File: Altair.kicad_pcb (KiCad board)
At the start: 2 copper layers, 224.3 x 12.5 mm, 135 parts, among them J1 Battery, SW1 SW_Push, SW10 SW_Push, SW11 SW_Push, SW12 SW_Push, SW13 SW_Push, SW14 SW_Push, SW15 SW_Push, SW16 SW_Push, SW17 SW_Push, SW18 SW_Push, SW19 SW_Push, SW2 SW_Push, SW20 SW_Push, SW21 SW_Push, SW22 SW_Push, SW23 SW_Push, SW24 SW_Push, SW25 SW_Push, SW26 SW_Push, SW27 SW_Push, SW28 SW_Push, SW29 SW_Push, SW3 SW_Push, SW30 SW_Push, SW31 SW_Push, SW32 SW_Push, SW33 SW_Push, SW34 SW_Push, SW35 SW_Push, SW36 SW_Push, SW37 SW_Push, SW38 SW_Push, SW39 SW_Push, SW4 SW_Push, SW40 SW_Push, SW41 SW_Push, SW42 SW_Push, SW43 SW_Push, SW44 SW_Push, SW45 SW_Push, SW46 SW_Push, SW47 SW_Push, SW48 SW_Push, SW49 SW_Push, SW5 SW_Push, SW50 SW_Push, SW51 SW_Push, SW52 SW_Push, SW53 SW_Push, SW54 SW_Push, SW55 SW_Push, SW56 SW_Push, SW57 SW_Push, SW58 SW_Push, SW59 SW_Push, SW6 SW_Push, SW60 SW_Push, SW61 SW_Push, SW62 SW_Push, SW63 SW_Push, SW64 SW_Push, SW7 SW_Push, SW8 SW_Push, SW9 SW_Push, SW97 RST, SW98 PWR, U1 nice_nano

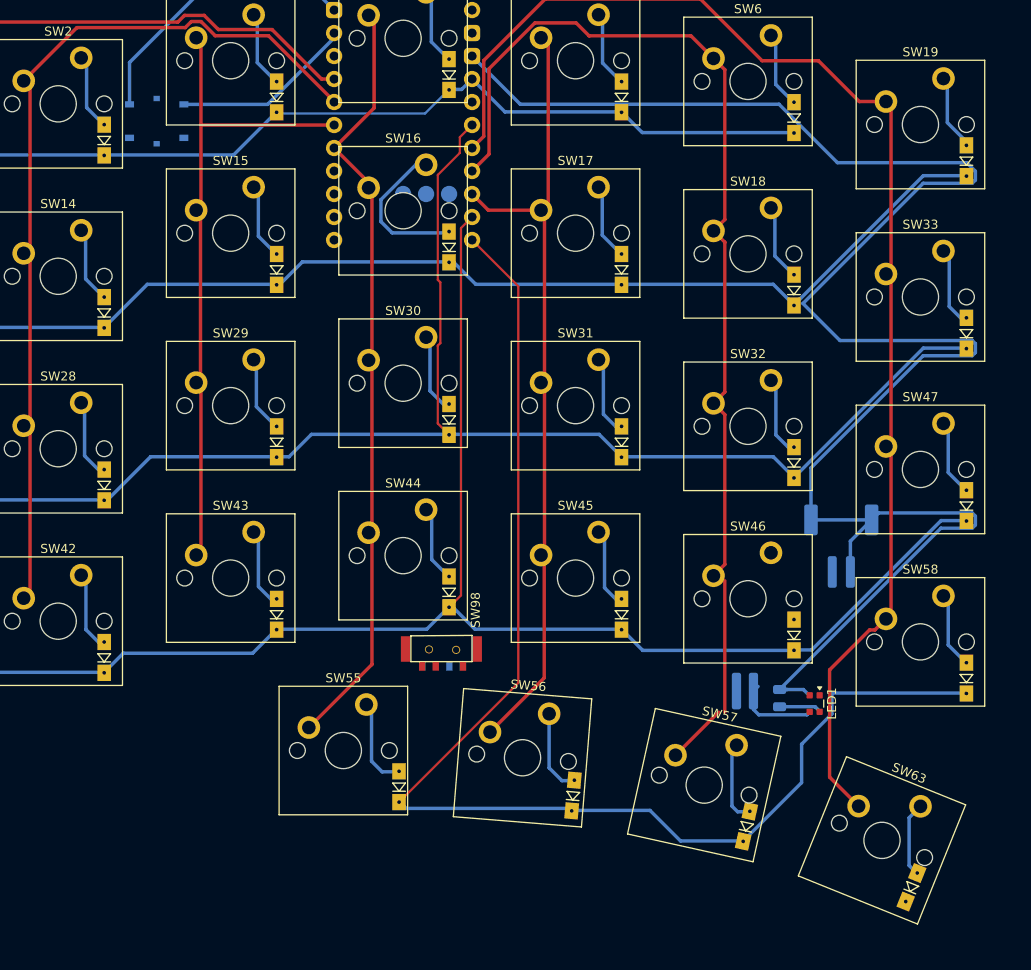
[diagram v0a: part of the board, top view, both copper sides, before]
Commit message: Remove Led
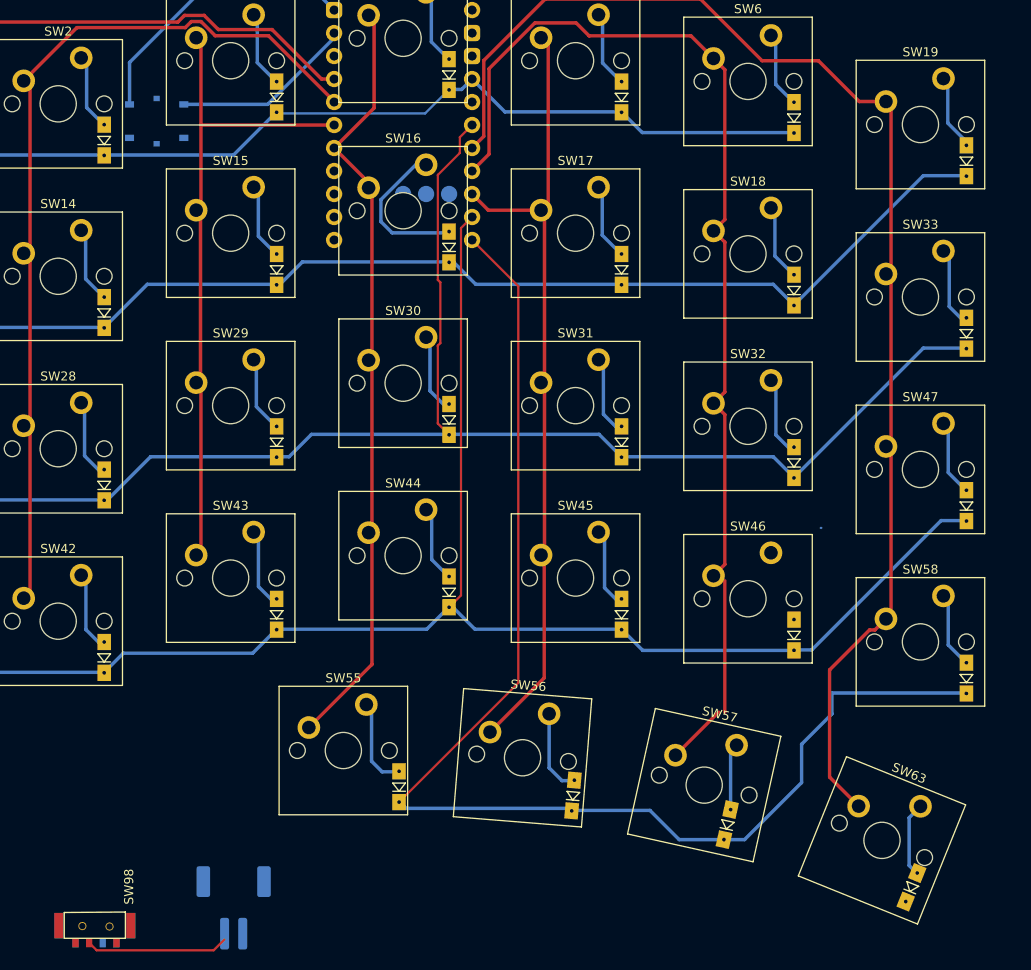
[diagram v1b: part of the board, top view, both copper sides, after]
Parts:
- removed C1: 0.1uF, Capacitor_SMD:C_0805_2012Metric
- removed LED1: WS2812_2020, PCM_marbastlib-various:LED_WS2812_2020
- removed R1: 300R, Resistor_SMD:R_0815_2038Metric
- moved J1 78.1 mm to (76.5, 126.9)
- moved SW98 49.0 mm to (65.1, 127.6)
- moved D57 2.13 mm to (131.1, 117.7)
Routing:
- net GND: track 230.2 -> 31.4 mm
- net Net-(J1-Pin_1): track 0.00 -> 15.8 mm
- net Net-(LED1-DIN): track 9.26 -> 0.00 mm
- net LED1+: track 4.62 -> 0.00 mm
- net N$57: track 9.16 -> 7.38 mm

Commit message: Remove onoff button
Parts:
- removed SW98: PWR, KLOTZ:MSK12C02_reversible
- moved J1 176.3 mm to (-8.38, -27.6), turned to 180 degrees
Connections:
- J1 pad 1: Net-(J1-Pin_1) -> +BATT
- U1 pad 16: LED1+ -> unconnected-(U1-3V3-Pad16)
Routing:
- net Net-(J1-Pin_1): track 15.8 -> 0.00 mm

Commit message: Change Diode Footprint to make new way routing
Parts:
- D1, D10, D11, D12, D13, D14, D15, D16, D17, D18, D19, D2, D20, D21, D22, D23, D24, D25, D26, D27, D28, D29, D3, D30, D31, D32, D33, D34, D35, D36, D37, D38, D39, D4, D40, D41, D42, D43, D44, D45, D46, D47, D48, D49, D5, D50, D51, D52, D53, D54, D55, D56, D57, D58, D59, D6, D60, D61, D62, D63, D64, D7, D8, D9: footprint KLOTZ:Diode_SOD123 -> Diode_SMD:D_SOD-123
- moved SW97 25.5 mm to (53.3, 19.2)
- moved D2 13.6 mm to (48.7, 40.3)
- moved D3 4.42 mm to (80.6, 41.7), turned to 180 degrees
- moved D1 3.69 mm to (46.4, 40.3)
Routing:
- net ROW3: track 169.4 -> 0.00 mm
- net ROW2: track 161.7 -> 0.00 mm
- net COL6: track 145.2 -> 0.00 mm
- net ROW4: track 144.6 -> 0.00 mm
- net ROW1: track 125.2 -> 0.00 mm
- net COL5: track 122.9 -> 0.00 mm
- net COL0: track 117.6 -> 0.00 mm
- net COL1: track 99.3 -> 0.00 mm
- net ROW0: track 101.3 -> 2.30 mm
- net COL4: track 89.1 -> 0.00 mm
- net COL3: track 86.2 -> 0.00 mm
- net COL2: track 73.2 -> 0.00 mm
- net GND: track 31.4 -> 0.00 mm
- net RST: track 20.2 -> 0.00 mm
- net N$16: track 17.1 -> 0.00 mm
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
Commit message: Done routing for SW
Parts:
- removed SW97: RST, PTS526_SMG15_SMTR2_LFS:SW_PTS526_SMG15_SMTR2_LFS
- moved J1 63.0 mm to (46.6, 3.15), turned to -90 degrees
- moved D47 14.4 mm to (144.0, 77.5)
- moved D19 14.3 mm to (144.0, 39.5)
- moved D58 14.2 mm to (144.0, 97.0)
- moved D33 14.2 mm to (144.0, 59.0)
- moved D14 13.2 mm to (49.0, 61.1)
- moved D28 13.2 mm to (49.0, 80.2)
- moved D42 13.2 mm to (49.0, 99.2)
- moved D3 4.25 mm to (81.3, 37.5), turned to 90 degrees
- moved D13 3.32 mm to (46.5, 61.1)
- moved D27 3.32 mm to (46.5, 80.2)
- moved D41 3.32 mm to (46.5, 99.2)
- moved D18 3.09 mm to (141.5, 59.0)
- moved D46 3.08 mm to (141.5, 97.0)
- moved D32 3.08 mm to (141.5, 77.5)
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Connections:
- D10 pad 1: ROW0 -> (no net)
- D11 pad 1: ROW0 -> (no net)
- D12 pad 1: ROW0 -> (no net)
- D19 pad 1: ROW1 -> ROW0
- D20 pad 1: ROW1 -> (no net)
- D21 pad 1: ROW1 -> (no net)
- D22 pad 1: ROW1 -> (no net)
- D23 pad 1: ROW1 -> (no net)
- D24 pad 1: ROW1 -> (no net)
- D25 pad 1: ROW1 -> (no net)
- D26 pad 1: ROW1 -> (no net)
- D33 pad 1: ROW2 -> ROW1
- D34 pad 1: ROW2 -> (no net)
- D35 pad 1: ROW2 -> (no net)
- D36 pad 1: ROW2 -> (no net)
- D37 pad 1: ROW2 -> (no net)
- D38 pad 1: ROW2 -> (no net)
- D39 pad 1: ROW2 -> (no net)
- D40 pad 1: ROW2 -> (no net)
- D47 pad 1: ROW3 -> ROW2
- D48 pad 1: ROW3 -> (no net)
- D49 pad 1: ROW3 -> (no net)
- D50 pad 1: ROW3 -> (no net)
- D51 pad 1: ROW3 -> (no net)
- D52 pad 1: ROW3 -> (no net)
- D53 pad 1: ROW3 -> (no net)
- D54 pad 1: ROW3 -> (no net)
- D58 pad 1: ROW4 -> ROW3
- D59 pad 1: ROW4 -> (no net)
- D60 pad 1: ROW4 -> (no net)
- D61 pad 1: ROW4 -> (no net)
- D62 pad 1: ROW4 -> (no net)
- D63 pad 1: ROW5 -> ROW4
- D7 pad 1: ROW0 -> (no net)
- D8 pad 1: ROW0 -> (no net)
- D9 pad 1: ROW0 -> (no net)
- U1 pad 12: ROW4 -> unconnected-(U1-P1.06-LF-Pad12)
- U1 pad 24: unconnected-(U1-P0.09-LF-Pad24) -> ROW4
- U1 pad 6: ROW1 -> ROW2
- U1 pad 7: ROW2 -> ROW1
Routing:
- net ROW4: track 0.00 -> 155.1 mm
- net ROW3: track 0.00 -> 149.4 mm, vias 0 -> 3
- net ROW2: track 0.00 -> 142.9 mm, vias 0 -> 4
- net COL6: track 0.00 -> 141.6 mm
- net ROW1: track 0.00 -> 123.3 mm, vias 0 -> 2
- net COL0: track 0.00 -> 116.3 mm
- net COL5: track 0.00 -> 109.0 mm, vias 0 -> 2
- net COL1: track 0.00 -> 92.5 mm, vias 0 -> 1
- net COL4: track 0.00 -> 87.4 mm
- net COL3: track 0.00 -> 81.4 mm
- net COL2: track 0.00 -> 76.3 mm
- net ROW0: track 2.30 -> 77.9 mm
- net N$42: track 0.00 -> 17.3 mm
- net N$28: track 0.00 -> 16.4 mm
- net N$14: track 0.00 -> 16.4 mm
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
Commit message: Done for 1 side PCB
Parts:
- moved J1 63.4 mm to (65.8, 63.6), turned to 180 degrees
- moved D16 1.83 mm to (98.5, 53.9)
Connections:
- U1 pad 12: unconnected-(U1-P1.06-LF-Pad12) -> ROW1
- U1 pad 13: unconnected-(U1-BAT+-Pad13) -> +BATT
- U1 pad 16: unconnected-(U1-3V3-Pad16) -> COL2
- U1 pad 17: COL0 -> COL1
- U1 pad 18: COL1 -> COL0
- U1 pad 19: COL2 -> COL3
- U1 pad 20: COL3 -> unconnected-(U1-P1.15-LF-Pad20)
- U1 pad 23: unconnected-(U1-P0.10-LF-Pad23) -> ROW2
- U1 pad 29: +BATT -> unconnected-(U1-BAT+-Pad29)
- U1 pad 6: ROW2 -> unconnected-(U1-P0.20-Pad6)
- U1 pad 7: ROW1 -> unconnected-(U1-P0.22-Pad7)
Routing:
- net GND: track 0.00 -> 66.3 mm, vias 0 -> 1
- net +BATT: track 0.00 -> 57.7 mm, vias 0 -> 1
- net ROW0: track 77.9 -> 102.6 mm
- net ROW1: track 123.3 -> 106.0 mm
- net ROW4: track 155.1 -> 138.9 mm, vias 0 -> 1
- net ROW2: track 142.9 -> 131.5 mm, vias 4 -> 1
- net COL5: track 109.0 -> 118.7 mm, vias 2 -> 1
- net COL6: track 141.6 -> 136.4 mm, vias 0 -> 1
- net COL3: track 81.4 -> 86.3 mm
- net COL1: track 92.5 -> 95.6 mm, vias 1 -> 2
- net COL2: track 76.3 -> 74.0 mm
- net N$6: track 11.8 -> 9.63 mm
- net COL0: track 116.3 -> 114.3 mm, vias 0 -> 2
- net N$46: track 11.8 -> 9.98 mm
- net N$18: track 11.9 -> 10.1 mm
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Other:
- board size 224.3 x 12.5 mm -> 133.4 x 110.6 mm

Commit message: add 2 MCU
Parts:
- added J2: Battery, Connector_JST:JST_PH_S2B-PH-SM4-TB_1x02-1MP_P2.00mm_Horizontal, F.Cu at (278.1, -17.6)
- added U2: SuperMini nRF52840, marbastlib-xp-promicroish:SuperMini_nRF52840_AH_USBdn, F.Cu at (238.8, 53.4)
- U1: value nice_nano -> SuperMini nRF52840; footprint PCM_marbastlib-xp-promicroish:nice_nano_AH_USBup -> marbastlib-xp-promicroish:SuperMini_nRF52840_AH_USBdn; moved to F.Cu
- moved J1 85.1 mm to (125.0, 2.30)
- moved D21 22.7 mm to (192.4, 73.2)
- moved D49 22.6 mm to (192.4, 111.2)
- moved D26 22.4 mm to (287.8, 75.4)
- moved D40 22.4 mm to (287.8, 94.4)
- moved D54 22.4 mm to (287.8, 113.5)
- moved D7 22.4 mm to (192.4, 53.7)
- moved D35 22.4 mm to (192.4, 91.7)
- moved D12 21.3 mm to (287.8, 54.5)
- moved D56 15.9 mm to (107.4, 128.9)
- moved D64 14.8 mm to (192.0, 135.1)
- moved D57 14.8 mm to (127.0, 131.9)
- moved D9 14.8 mm to (243.9, 49.1)
- moved SW22 14.8 mm to (219.7, 66.6)
- moved SW24 14.8 mm to (257.8, 66.6)
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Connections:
- D64 pad 1: ROW5 -> (no net)
- U1 pad 10: COL4 -> ROW3
- U1 pad 11: ROW3 -> unconnected-(U1-P1.04-LF-Pad11)
- U1 pad 12: ROW1 -> ROW4
- U1 pad 13: +BATT -> GND
- U1 pad 14: GND -> unconnected-(U1-GND-Pad14)
- U1 pad 15: RST -> unconnected-(U1-RST-Pad15)
- U1 pad 16: COL2 -> unconnected-(U1-3V3-Pad16)
- U1 pad 17: COL1 -> ROW0
- U1 pad 18: COL0 -> unconnected-(U1-P0.29-LF-Pad18)
- U1 pad 19: COL3 -> COL2
- U1 pad 20: unconnected-(U1-P1.15-LF-Pad20) -> COL1
- U1 pad 21: unconnected-(U1-P1.13-LF-Pad21) -> COL0
- U1 pad 22: unconnected-(U1-P1.11-LF-Pad22) -> COL3
- U1 pad 23: ROW2 -> ROW1
- U1 pad 24: ROW4 -> ROW2
- U1 pad 28: GND -> unconnected-(U1-GND-Pad28)
- U1 pad 29: unconnected-(U1-BAT+-Pad29) -> +BATT
- U1 pad 3: GND -> unconnected-(U1-GND-Pad3)
- U1 pad 4: GND -> unconnected-(U1-GND-Pad4)
- U1 pad 5: ROW0 -> unconnected-(U1-P0.17-Pad5)
- U1 pad 7: unconnected-(U1-P0.22-Pad7) -> COL5
- U1 pad 9: COL5 -> COL4
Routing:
- net (no net): track 0.00 -> 471.2 mm
- net COL8: track 0.00 -> 105.3 mm
- net COL11: track 0.00 -> 81.4 mm
- net COL9: track 0.00 -> 80.4 mm
- net COL10: track 0.00 -> 79.7 mm
- net GND: track 66.3 -> 0.00 mm, vias 1 -> 0
- net +BATT: track 57.7 -> 0.00 mm, vias 1 -> 0
- net COL12: track 0.00 -> 57.2 mm
- net COL14: track 0.00 -> 57.1 mm
- net COL13: track 0.00 -> 57.1 mm
- net N$21: track 0.00 -> 15.8 mm
- net N$49: track 0.00 -> 15.7 mm
- net N$40: track 0.00 -> 15.4 mm
- net N$26: track 0.00 -> 15.4 mm
- net N$54: track 0.00 -> 15.4 mm
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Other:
- board outline removed
